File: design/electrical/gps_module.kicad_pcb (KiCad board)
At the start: 2 copper layers, 90.2 x 95.9 mm, 21 parts, among them IC1 ATMEGA16M1-A, J1 SMA, U1 TPS2030, U2 LM1117-3.3, U3 RXM-GPS-RM, U4 ADG787, U5 ATA6561, U6 ATA6561

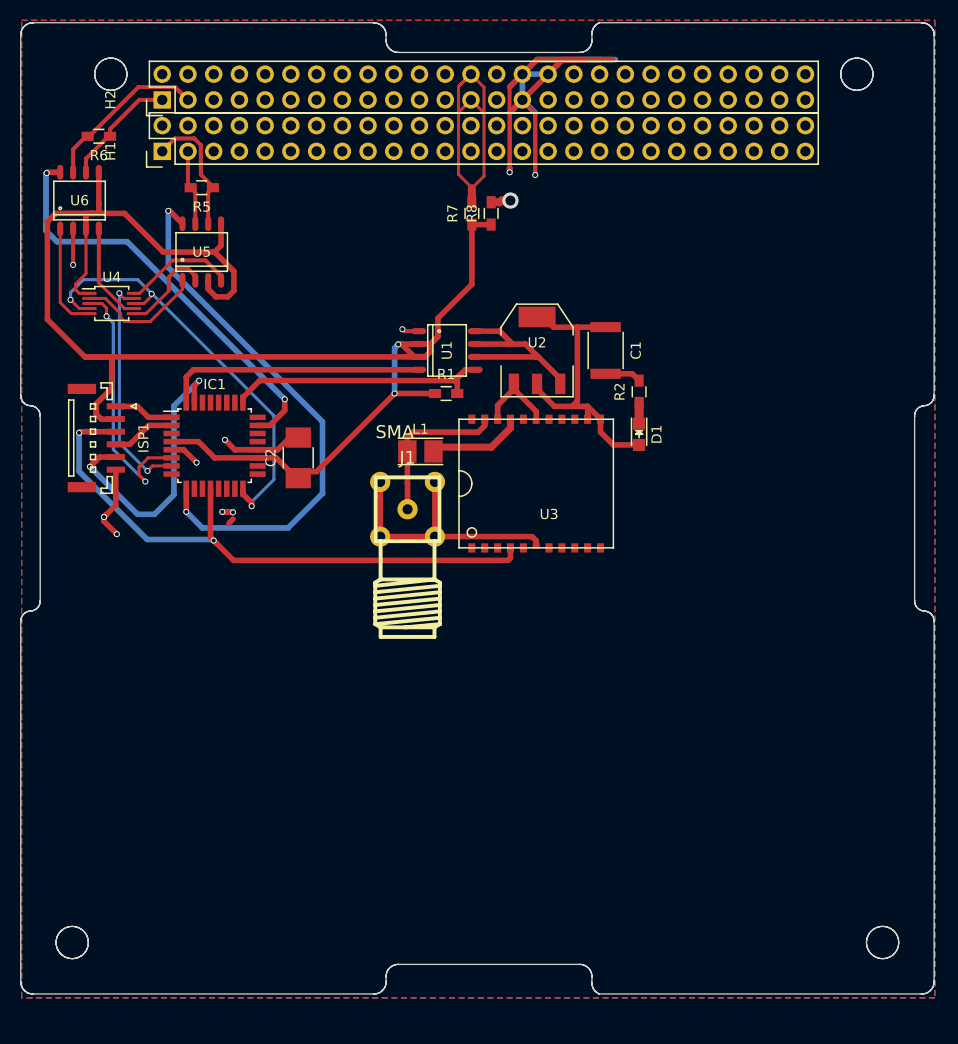
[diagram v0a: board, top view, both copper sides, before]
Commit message: add 3v3 converter and LEDs
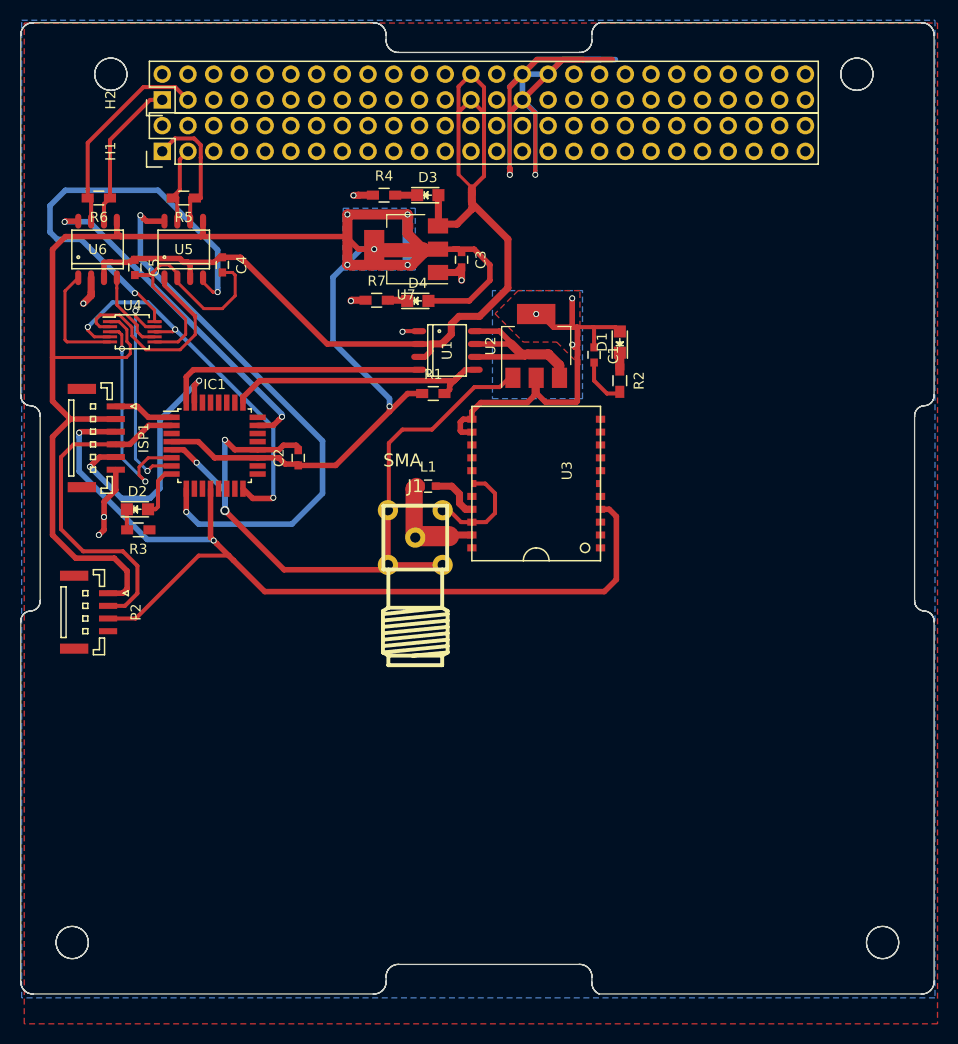
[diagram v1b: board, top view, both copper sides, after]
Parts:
- removed R8: DNP, Resistors_SMD:R_0603_HandSoldering
- added C3: 1uF, Capacitors_SMD:C_0603, F.Cu at (108.2, 75.7)
- added C4: 1uF, Capacitors_SMD:C_0603, F.Cu at (84.6, 76.2)
- added C5: 1uF, Capacitors_SMD:C_0603, F.Cu at (75.9, 76.5)
- added D2: Led_Small, LEDs:LED_0805, F.Cu at (76.2, 100.3)
- added D3: Led_Small, LEDs:LED_0805, F.Cu at (104.9, 69.3)
- added D4: Led_Small, LEDs:LED_0805, F.Cu at (103.9, 79.8)
- added P2: CONN_01X04, Connectors_JST:JST_GH_BM04B-GHS-TBT_04x1.25mm_Straight, F.Cu at (71.6, 110.5)
- added R3: 1k, Resistors_SMD:R_0603_HandSoldering, F.Cu at (76.3, 102.4)
- added R4: 1k, Resistors_SMD:R_0603_HandSoldering, F.Cu at (100.6, 69.3)
- added U7: LM1117-3.3, TO_SOT_Packages_SMD:SOT-223, F.Cu at (102.7, 74.7)
- C1: footprint Capacitors_SMD:C_1812 -> Capacitors_SMD:C_0603
- C2: footprint Capacitors_SMD:C_1210_HandSoldering -> Capacitors_SMD:C_0603
- L1: footprint Inductors:Inductor_Taiyo-Yuden_NR-24xx_HandSoldering -> Capacitors_SMD:C_0603
- R7: value 0 -> 1k
- moved R7 12.7 mm to (99.8, 79.7), turned to 0 degrees
- moved D1 9.31 mm to (123.8, 83.8), turned to 90 degrees
- moved R6 6.10 mm to (72.4, 69.6)
- moved U6 5.14 mm to (72.3, 74.7)
- moved L1 3.51 mm to (104.9, 98.0)
- moved U4 3.45 mm to (75.7, 82.8)
- moved J1 2.90 mm to (103.6, 103.1)
- moved R2 2.20 mm to (123.8, 87.6), turned to 270 degrees
- moved R5 2.05 mm to (80.8, 69.6)
- moved U5 1.80 mm to (80.8, 74.7)
- moved R1 1.27 mm to (105.4, 88.9)
- moved C1 1.23 mm to (121.3, 85.1)
- moved U2 0.45 mm to (115.6, 84.2), turned to 90 degrees
- turned U3 to 90 degrees
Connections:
- net Net-(C1-Pad1) renamed /3V3_GPS
- C2 pad 1: +5V -> +3V3
- IC1 pad 19: +5V -> +3V3
- IC1 pad 4: +5V -> +3V3
- ISP1 pad 2: +5V -> +3V3
- R1 pad 1: +5V -> +3V3
- R7 pad 1: +5V -> GND
- R7 pad 2: 5V_BUS -> Net-(D4-Pad1)
- U1 pad 2: +5V -> 5V_BUS
- U1 pad 3: +5V -> 5V_BUS
- U4 pad 1: +5V -> +3V3
- U5 pad 3: +5V -> 5V_BUS
- U5 pad 5: +5V -> +3V3
- U6 pad 3: +5V -> 5V_BUS
- U6 pad 5: +5V -> +3V3
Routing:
- net +3V3: track 0.00 -> 194.9 mm, vias 0 -> 6
- net +5V: track 161.5 -> 0.00 mm, vias 2 -> 0
- net 5V_BUS: track 32.9 -> 103.8 mm
- net GND: track 148.9 -> 212.1 mm, vias 8 -> 12
- net GPS_TX: track 60.0 -> 93.7 mm
- net Net-(U4-Pad10): track 11.0 -> 44.3 mm, vias 0 -> 2
- net Net-(IC1-Pad2): track 6.88 -> 35.1 mm
- net /3V3_GPS: track 29.7 -> 40.2 mm, vias 0 -> 3
- net Net-(U4-Pad2): track 13.0 -> 21.3 mm
- net CAN2_STBY: track 42.0 -> 33.7 mm
- net Net-(D2-Pad2): track 0.00 -> 5.25 mm
- net Net-(J1-Pad1): track 15.8 -> 11.3 mm
- net Net-(L1-Pad2): track 9.43 -> 5.07 mm
- net CAN2_H: track 16.7 -> 20.7 mm
- net TX_CAN: track 25.9 -> 22.0 mm
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- added copper zone on B.Cu, net +3V3
- added copper zone on F.Cu, net +3V3
- added copper zone on B.Cu, net /3V3_GPS
- added copper zone on F.Cu, net /3V3_GPS
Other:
- net class Default: trace_width 0.4 -> 0.7
